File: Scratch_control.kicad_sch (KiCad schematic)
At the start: 40 parts, among them J1 OUTPUT1, J2 OUTPUT2, J3 OUTPUT3, J4 Conn_01x02, J5 Conn_01x04, K1 Key, K2 Key, K3 Key, K4 Key, U1 AMS1117-3.3, U2 TPS54540, U3 STM32G030F6Px, X1 8M

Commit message: Update whole project.Delete some useless pin and so on....
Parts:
- removed C13: 22pF, Capacitor_SMD:C_0603_1608Metric, symbol Basic_passive_components:Capacitor
- removed J1: OUTPUT1, Connector_JST:JST_GH_SM05B-GHS-TB_1x05-1MP_P1.25mm_Horizontal, symbol Connector_Generic_MountingPin:Conn_01x05_MountingPin
- removed J2: OUTPUT2, Connector_JST:JST_GH_SM05B-GHS-TB_1x05-1MP_P1.25mm_Horizontal, symbol Connector_Generic_MountingPin:Conn_01x05_MountingPin
- removed J3: OUTPUT3, Connector_JST:JST_GH_SM05B-GHS-TB_1x05-1MP_P1.25mm_Horizontal, symbol Connector_Generic_MountingPin:Conn_01x05_MountingPin
- removed X1: 8M, Crystal:Crystal_HC49-U_Vertical, symbol Basic_crystal_and_oscillator:Xtal-2
- added C13: 47uF, Capacitor_SMD:CP_Elec_8x10, symbol Device:C_Polarized
- added J1: MG995, Connector_PinHeader_2.54mm:PinHeader_1x03_P2.54mm_Horizontal, symbol Connector_Generic:Conn_01x03
- added J2: LED, Connector_PinHeader_2.54mm:PinHeader_1x03_P2.54mm_Horizontal, symbol Connector_Generic:Conn_01x03
- added J3: SENSOR, Connector_JST:JST_GH_SM03B-GHS-TB_1x03-1MP_P1.25mm_Horizontal, symbol Connector_Generic_MountingPin:Conn_01x03_MountingPin
- added K4: Key, Button_Switch_SMD:SW_DIP_SPSTx01_Slide_6.7x4.1mm_W6.73mm_P2.54mm_LowProfile_JPin, symbol Basic_passive_components:Key
- added R11: 10k, Resistor_SMD:R_0603_1608Metric, symbol Basic_passive_components:Resistor
- C11: value 47uF -> 100nF; footprint Capacitor_SMD:C_0805_2012Metric -> Capacitor_SMD:C_0603_1608Metric
- C12: value 22pF -> 100nF
- R8: value 11.5k -> 20k
- R9: value 60.4k -> 105k
- renumbered K4 to RST1
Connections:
- net SENSOR1 is gone; now on net KEY3: U3.9 (PA2)
- net +24V: now also C13.1; no longer C11.2
- net +3V3: now also C12.2, J5.4, R11.1; no longer J5.1
- net +5V: now also J1.2 (Pin_2), J2.1 (Pin_1), J3.3 (Pin_3)
- net GND: now also J5.1, C13.2, J1.3 (Pin_3), J2.3 (Pin_3), J3.1 (Pin_1), J3.MP (MountPin), K4.2; no longer J5.4
- net KEY3: no longer U3.12 (PA5)
- net PWM3: now also J2.2 (Pin_2)
- net PWM4: now also J1.1 (Pin_1)
- net SWCLK: now also J5.2; no longer J5.3
- net SWDIO: now also J5.3; no longer J5.2
- net at U3.2 (PB9/PC14): no longer C12.2
- net PWM1: no longer names the net of U3.11 (PA4)
- net PWM2 renamed SENSOR
- net SENSOR: now also J3.2 (Pin_2)
- net PWM5: no longer names the net of U3.16 (PA11/PA9)
- net PWM6: no longer names the net of U3.20 (PB3/PB4/PB5/PB6)
- net SENSOR2 renamed KEY4
- net KEY4: now also C11.2, K4.1, R11.2
- net SENSOR3: no longer names the net of U3.1 (PB7/PB8)
- no-connect marks 1 -> 8
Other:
- moved on the sheet: J5

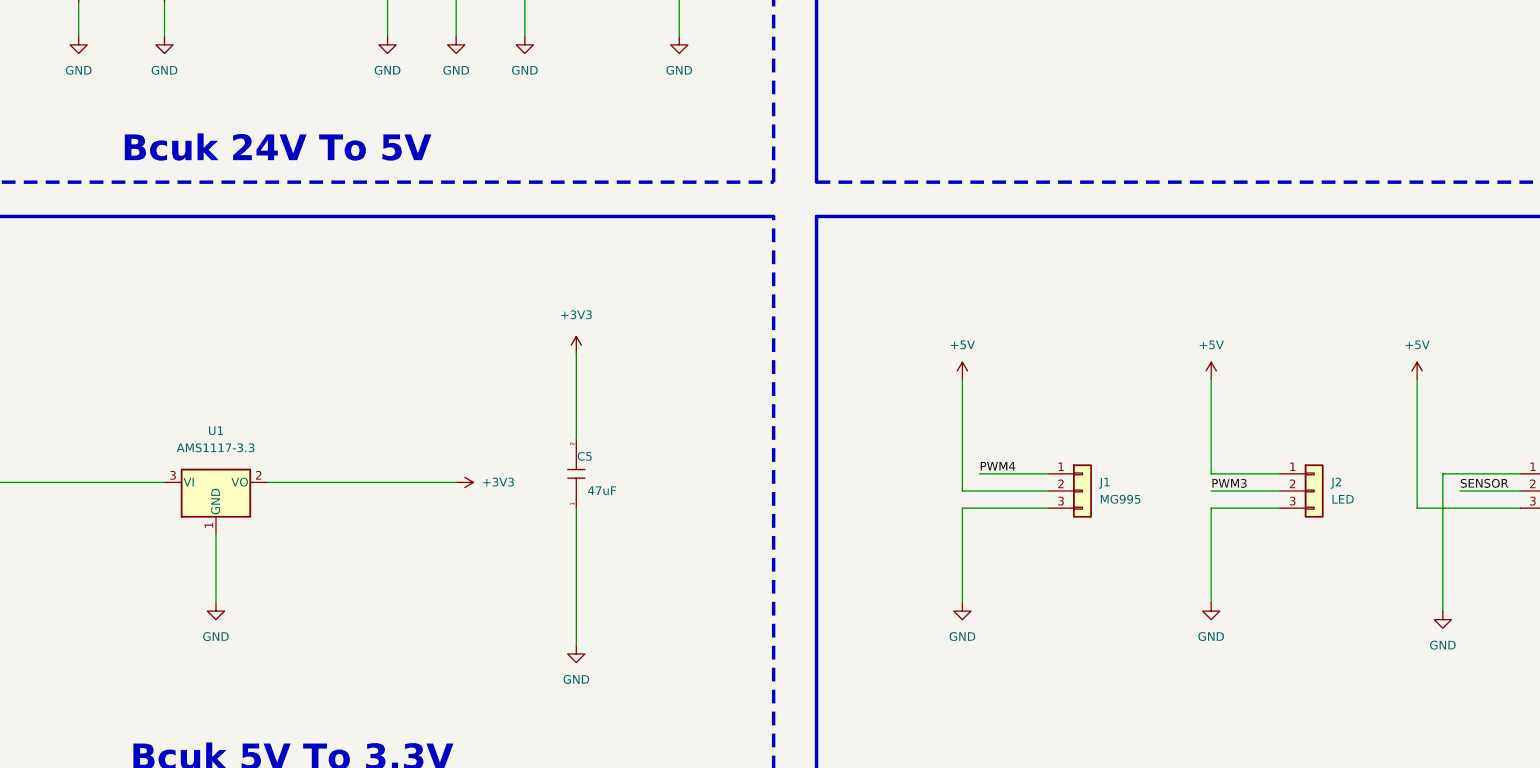
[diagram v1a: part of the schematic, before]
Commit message: add some decoupling capacitors
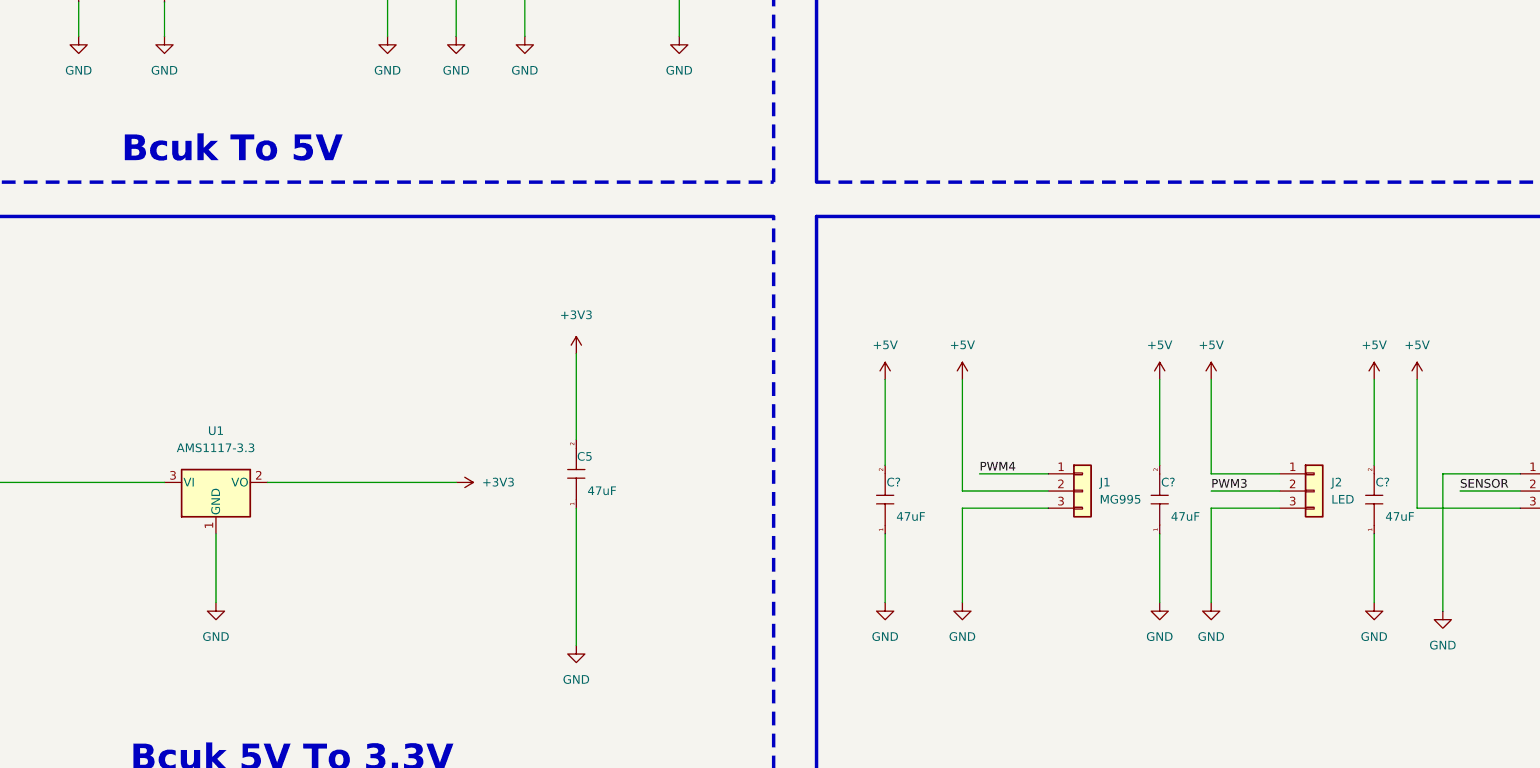
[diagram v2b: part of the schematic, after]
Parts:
- added C? (x3): 47uF, Capacitor_SMD:C_0603_1608Metric, symbol Basic_passive_components:Capacitor
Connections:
- net +5V: now also C?.2, C?.2, C?.2
- net GND: now also C?.1, C?.1, C?.1
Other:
- note added: "Bcuk To 5V"
- note removed: "Bcuk 24V To 5V"
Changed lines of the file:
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@@
+    (stroke (width 0) (type default) (color 0 0 0 0))
+  )
+  (wire (pts (xy 217.17 152.4) (xy 217.17 162.56))
     (stroke (width 0) (type default) (color 0 0 0 0))
   )
   (wire (pts (xy 379.73 140.97) (xy 388.62 140.97))
+    (stroke (width 0) (type default) (color 0 0 0 0))
+  )
+  (wire (pts (xy 176.53 152.4) (xy 176.53 162.56))
     (stroke (width 0) (type default) (color 0 0 0 0))
   )
@@
     (stroke (width 0) (type default) (color 0 0 0 0))
   )
+  (wire (pts (xy 248.92 152.4) (xy 248.92 162.56))
+    (stroke (width 0) (type default) (color 0 0 0 0))
+  )
   (wire (pts (xy 43.18 44.45) (xy 57.15 44.45))
     (stroke (width 0) (type default) (color 0 0 0 0))
@@
     (stroke (width 0) (type default) (color 0 0 0 0))
   )
+  (wire (pts (xy 217.17 129.54) (xy 217.17 142.24))
+    (stroke (width 0) (type default) (color 0 0 0 0))
+  )
   (wire (pts (xy 341.63 45.72) (xy 354.33 45.72))
     (stroke (width 0) (type default) (color 0 0 0 0))
@@
     (stroke (width 0) (type default) (color 0 0 0 0))
   )
+  (wire (pts (xy 248.92 129.54) (xy 248.92 142.24))
+    (stroke (width 0) (type default) (color 0 0 0 0))
+  )
   (wire (pts (xy 187.96 148.59) (xy 187.96 162.56))
     (stroke (width 0) (type default) (color 0 0 0 0))
@@
   )
   (wire (pts (xy 43.18 73.66) (xy 43.18 78.74))
+    (stroke (width 0) (type default) (color 0 0 0 0))
+  )
+  (wire (pts (xy 176.53 129.54) (xy 176.53 142.24))
     (stroke (width 0) (type default) (color 0 0 0 0))
   )
@@
     (effects (font (size 3.81 3.81) (thickness 0.762) bold) (justify left bottom))
   )
-  (text "Bcuk 24V To 5V" (at 63.5 97.79 0)
+  (text "Bcuk To 5V" (at 63.5 97.79 0)
     (effects (font (size 3.81 3.81) (thickness 0.762) bold) (justify left bottom))
   )
@@
     (pin "2")
   )
+  (symbol (lib_id "power:GND") (at 217.17 162.56 0) (unit 1)
+    (in_bom yes) (on_board yes) (fields_autoplaced)
+    (property "Reference" "#PWR?" (id 0) (at 217.17 168.91 0)
+      (effects (font (size 1.27 1.27)) hide)
+    )
+    (property "Value" "GND" (id 1) (at 217.17 167.64 0))
+    (property "Footprint" "" (id 2) (at 217.17 162.56 0)
+      (effects (font (size 1.27 1.27)) hide)
+    )
+    (property "Datasheet" "" (id 3) (at 217.17 162.56 0)
+      (effects (font (size 1.27 1.27)) hide)
+    )
+    (pin "1")
+  )
   (symbol (lib_id "Basic_passive_components:Resistor") (at 43.18 54.61 270) (unit 1)
     (in_bom yes) (on_board yes)
@@
     (pin "2")
   )
+  (symbol (lib_id "power:GND") (at 176.53 162.56 0) (unit 1)
+    (in_bom yes) (on_board yes) (fields_autoplaced)
+    (property "Reference" "#PWR?" (id 0) (at 176.53 168.91 0)
+      (effects (font (size 1.27 1.27)) hide)
+    )
+    (property "Value" "GND" (id 1) (at 176.53 167.64 0))
+    (property "Footprint" "" (id 2) (at 176.53 162.56 0)
+      (effects (font (size 1.27 1.27)) hide)
+    )
+    (property "Datasheet" "" (id 3) (at 176.53 162.56 0)
+      (effects (font (size 1.27 1.27)) hide)
+    )
+    (pin "1")
+  )
   (symbol (lib_id "power:GND") (at 30.48 80.01 0) (unit 1)
     (in_bom yes) (on_board yes) (fields_autoplaced)
@@
     (pin "1")
   )
+  (symbol (lib_id "power:+5V") (at 176.53 129.54 0) (unit 1)
+    (in_bom yes) (on_board yes) (fields_autoplaced)
+    (property "Reference" "#PWR?" (id 0) (at 176.53 133.35 0)
+      (effects (font (size 1.27 1.27)) hide)
+    )
+    (property "Value" "+5V" (id 1) (at 176.53 124.46 0))
+    (property "Footprint" "" (id 2) (at 176.53 129.54 0)
+      (effects (font (size 1.27 1.27)) hide)
+    )
+    (property "Datasheet" "" (id 3) (at 176.53 129.54 0)
+      (effects (font (size 1.27 1.27)) hide)
+    )
+    (pin "1")
+  )
   (symbol (lib_id "power:GND") (at 43.18 78.74 0) (unit 1)
     (in_bom yes) (on_board yes) (fields_autoplaced)
@@
     )
     (property "Datasheet" "" (id 3) (at 302.26 139.7 0)
+      (effects (font (size 1.27 1.27)) hide)
+    )
+    (pin "1")
+  )
+  (symbol (lib_id "power:+5V") (at 217.17 129.54 0) (unit 1)
+    (in_bom yes) (on_board yes) (fields_autoplaced)
+    (property "Reference" "#PWR?" (id 0) (at 217.17 133.35 0)
+      (effects (font (size 1.27 1.27)) hide)
+    )
+    (property "Value" "+5V" (id 1) (at 217.17 124.46 0))
+    (property "Footprint" "" (id 2) (at 217.17 129.54 0)
+      (effects (font (size 1.27 1.27)) hide)
+    )
+    (property "Datasheet" "" (id 3) (at 217.17 129.54 0)
       (effects (font (size 1.27 1.27)) hide)
     )
@@
     (pin "2")
     (pin "3")
+  )
+  (symbol (lib_id "power:GND") (at 248.92 162.56 0) (unit 1)
+    (in_bom yes) (on_board yes) (fields_autoplaced)
+    (property "Reference" "#PWR?" (id 0) (at 248.92 168.91 0)
+      (effects (font (size 1.27 1.27)) hide)
+    )
+    (property "Value" "GND" (id 1) (at 248.92 167.64 0))
+    (property "Footprint" "" (id 2) (at 248.92 162.56 0)
+      (effects (font (size 1.27 1.27)) hide)
+    )
+    (property "Datasheet" "" (id 3) (at 248.92 162.56 0)
+      (effects (font (size 1.27 1.27)) hide)
+    )
+    (pin "1")
   )
   (symbol (lib_id "Integrated-circuit_micro-controller:STM32G030F6Px") (at 331.47 45.72 0) (unit 2)
@@
     (pin "1")
   )
+  (symbol (lib_id "power:+5V") (at 248.92 129.54 0) (unit 1)
+    (in_bom yes) (on_board yes) (fields_autoplaced)
+    (property "Reference" "#PWR?" (id 0) (at 248.92 133.35 0)
+      (effects (font (size 1.27 1.27)) hide)
+    )
+    (property "Value" "+5V" (id 1) (at 248.92 124.46 0))
+    (property "Footprint" "" (id 2) (at 248.92 129.54 0)
+      (effects (font (size 1.27 1.27)) hide)
+    )
+    (property "Datasheet" "" (id 3) (at 248.92 129.54 0)
+      (effects (font (size 1.27 1.27)) hide)
+    )
+    (pin "1")
+  )
   (symbol (lib_id "power:GND") (at 148.59 273.05 0) (unit 1)
     (in_bom yes) (on_board yes) (fields_autoplaced)
@@
     (pin "1")
   )
+  (symbol (lib_id "Basic_passive_components:Capacitor") (at 217.17 147.32 90) (unit 1)
+    (in_bom yes) (on_board yes)
+    (property "Reference" "C?" (id 0) (at 218.44 144.78 90))
+    (property "Value" "47uF" (id 1) (at 220.98 149.86 90))
+    (property "Footprint" "Capacitor_SMD:C_0603_1608Metric" (id 2) (at 217.17 147.32 0)
+      (effects (font (size 1.27 1.27)) hide)
+    )
+    (property "Datasheet" "" (id 3) (at 217.17 147.32 0)
+      (effects (font (size 1.27 1.27)) hide)
+    )
+    (pin "1")
+    (pin "2")
+  )
   (symbol (lib_id "Connector_Generic:Conn_01x02") (at 335.28 143.51 0) (unit 1)
     (in_bom yes) (on_board yes) (fields_autoplaced)
@@
     )
     (pin "1")
+  )
+  (symbol (lib_id "Basic_passive_components:Capacitor") (at 176.53 147.32 90) (unit 1)
+    (in_bom yes) (on_board yes)
+    (property "Reference" "C?" (id 0) (at 177.8 144.78 90))
+    (property "Value" "47uF" (id 1) (at 180.34 149.86 90))
+    (property "Footprint" "Capacitor_SMD:C_0603_1608Metric" (id 2) (at 176.53 147.32 0)
+      (effects (font (size 1.27 1.27)) hide)
+    )
+    (property "Datasheet" "" (id 3) (at 176.53 147.32 0)
+      (effects (font (size 1.27 1.27)) hide)
+    )
+    (pin "1")
+    (pin "2")
   )
   (symbol (lib_id "power:+5V") (at 187.96 129.54 0) (unit 1)
@@
     )
     (property "Datasheet" "" (id 3) (at 102.87 232.41 0)
+      (effects (font (size 1.27 1.27)) hide)
+    )
+    (pin "1")
+    (pin "2")
+  )
+  (symbol (lib_id "Basic_passive_components:Capacitor") (at 248.92 147.32 90) (unit 1)
+    (in_bom yes) (on_board yes)
+    (property "Reference" "C?" (id 0) (at 250.19 144.78 90))
+    (property "Value" "47uF" (id 1) (at 252.73 149.86 90))
+    (property "Footprint" "Capacitor_SMD:C_0603_1608Metric" (id 2) (at 248.92 147.32 0)
+      (effects (font (size 1.27 1.27)) hide)
+    )
+    (property "Datasheet" "" (id 3) (at 248.92 147.32 0)
       (effects (font (size 1.27 1.27)) hide)
     )
@@
       (reference "#PWR043") (unit 1) (value "GND") (footprint "")
     )
+    (path "/279a623f-c2c8-4fd6-8610-cba385021b02"
+      (reference "#PWR?") (unit 1) (value "GND") (footprint "")
+    )
+    (path "/4e74f20b-7b6a-478f-94a4-2264c355e8c9"
+      (reference "#PWR?") (unit 1) (value "GND") (footprint "")
+    )
+    (path "/580cc2b1-ae9d-4b18-8f0a-38b8f1133583"
+      (reference "#PWR?") (unit 1) (value "+5V") (footprint "")
+    )
+    (path "/6b2dcf93-3667-4f47-b9a6-532be846a547"
+      (reference "#PWR?") (unit 1) (value "+5V") (footprint "")
+    )
+    (path "/826c0091-ca06-409f-ad38-99fc1772e851"
+      (reference "#PWR?") (unit 1) (value "GND") (footprint "")
+    )
+    (path "/8dec233a-0752-435a-ac74-e4d04d4ad52b"
+      (reference "#PWR?") (unit 1) (value "+5V") (footprint "")
+    )
     (path "/d932113b-9e28-4ff4-9adf-fe421ef62879"
       (reference "C1") (unit 1) (value "47uF") (footprint "Capacitor_SMD:C_0805_2012Metric")
@@
       (reference "C13") (unit 1) (value "47uF") (footprint "Capacitor_SMD:CP_Elec_8x10")
     )
+    (path "/9ac49f19-8b7c-4196-9c11-48f1bc8ef8cb"
+      (reference "C?") (unit 1) (value "47uF") (footprint "Capacitor_SMD:C_0603_1608Metric")
+    )
+    (path "/b6debd51-d17c-4230-8fc1-1e720e9b70ab"
+      (reference "C?") (unit 1) (value "47uF") (footprint "Capacitor_SMD:C_0603_1608Metric")
+    )
+    (path "/c10b06aa-7314-4cf9-8acb-ba149e9d8b82"
+      (reference "C?") (unit 1) (value "47uF") (footprint "Capacitor_SMD:C_0603_1608Metric")
+    )
     (path "/a1a694dc-0d1c-4f45-bf1f-ccb2691c3920"
